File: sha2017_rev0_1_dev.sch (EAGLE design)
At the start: 87 parts, among them IC1 AP7215, IC2 LM1117, IC3 CP210X_USB_UART, IC5 ESP32WROOM32, Q1 MMBT2222A, Q2 MMBT2222A, Q3 SI1304 BDL, SW100 MCMT5-F-V, X701 2908-05WB-MG

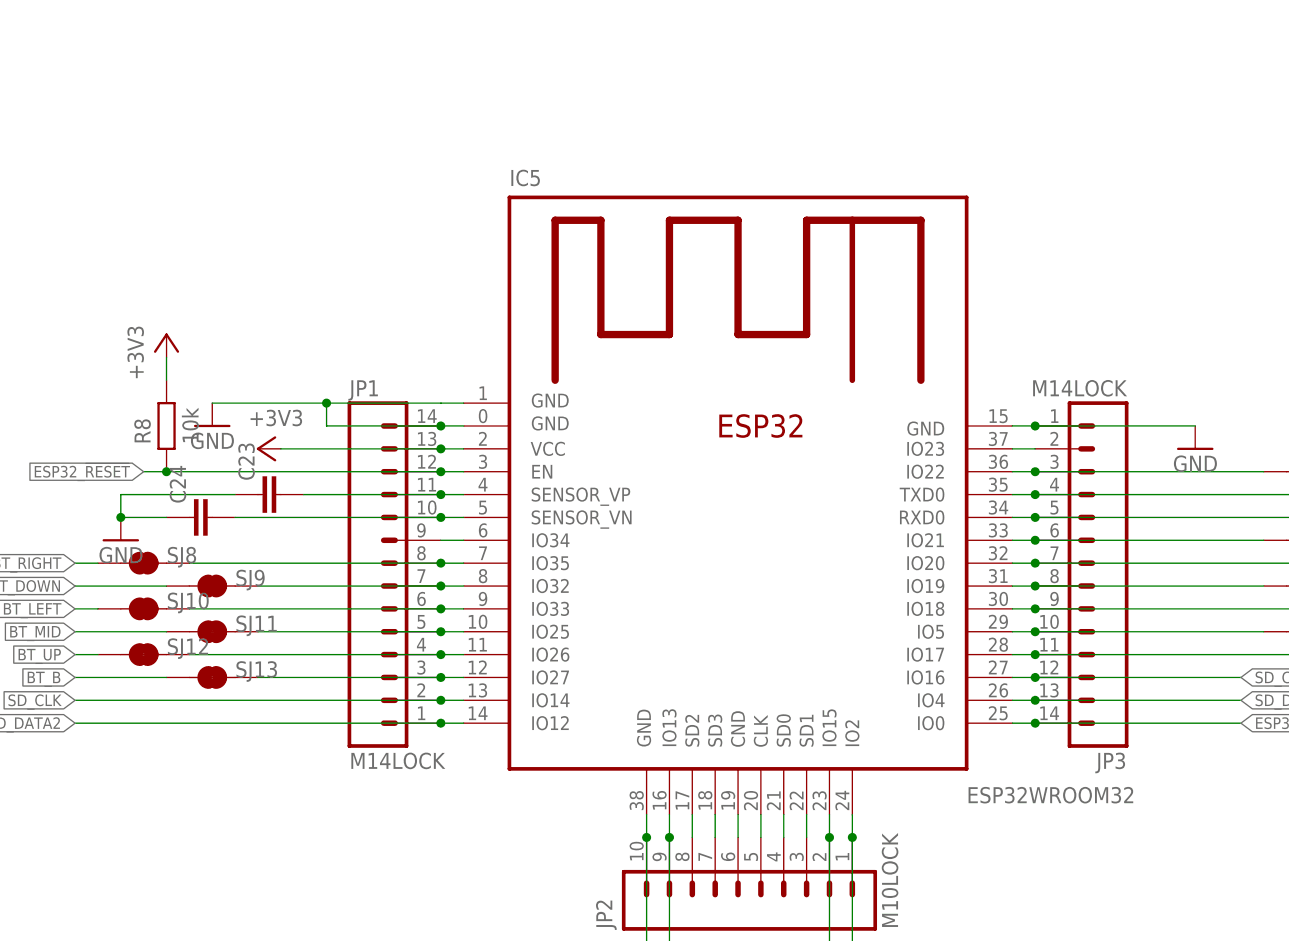
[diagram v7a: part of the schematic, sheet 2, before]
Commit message: fixed silkscreen
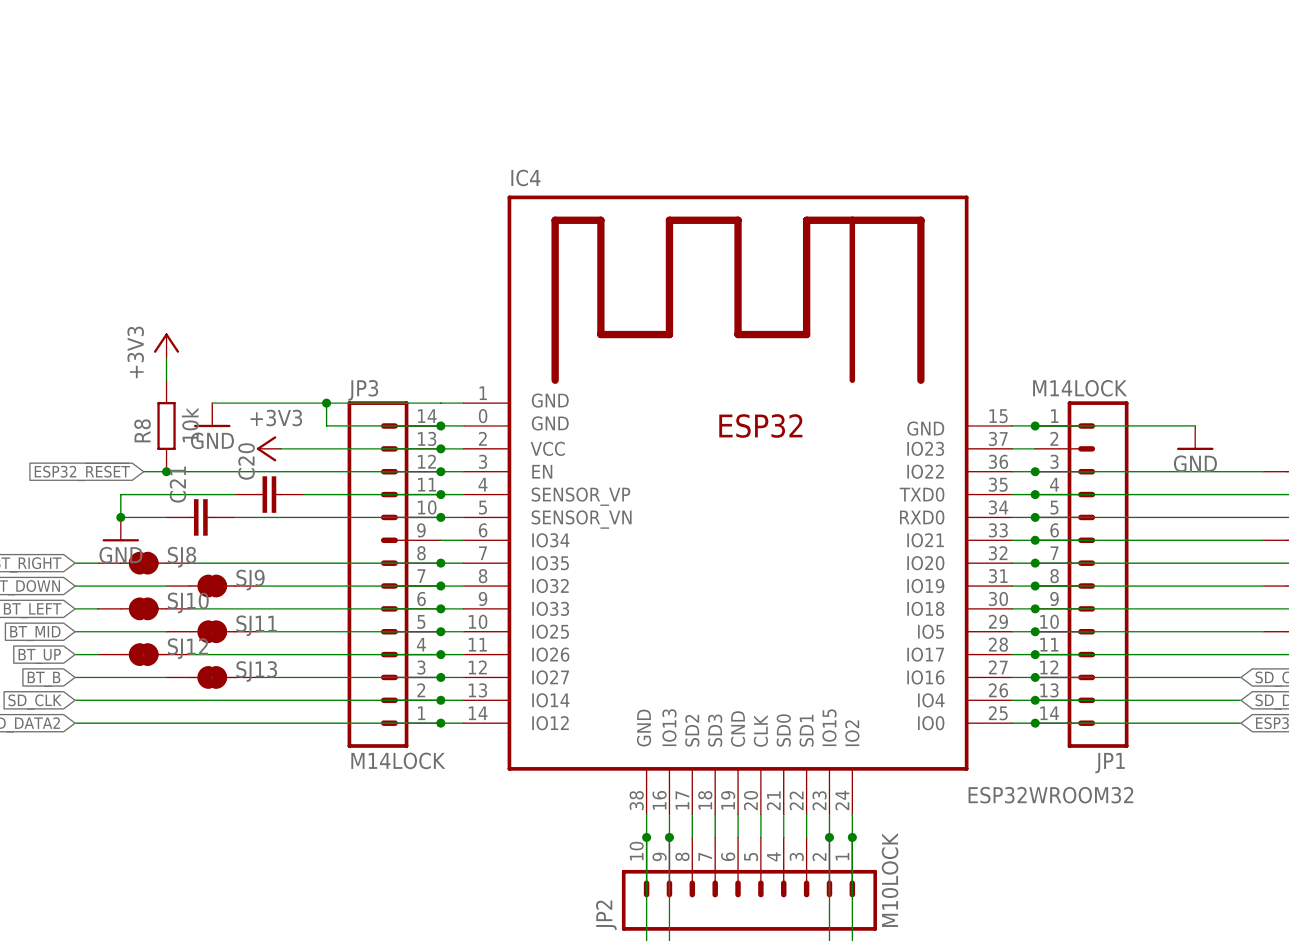
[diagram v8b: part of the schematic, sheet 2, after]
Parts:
- C20: value 100n -> (none); OC_FARNELL (none) -> unknown; PARTNO GRM188R71H104KA93D -> (none)
- C21: value 4u7/16V -> (none); device rcl:C-EUC0805 -> rcl:C-EUC0603; OC_FARNELL (none) -> unknown; PARTNO GRM21BR61C475KA88K -> (none)
- C23: value (none) -> 4u7/16V; device rcl:C-EUC0603 -> rcl:C-EUC0805; OC_FARNELL unknown -> (none); PARTNO (none) -> GRM21BR61C475KA88K
- C24: value (none) -> 100n; OC_FARNELL unknown -> (none); PARTNO (none) -> GRM188R71H104KA93D
- renumbered D100 to D8, IC5 to IC4
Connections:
- net +3V3: now also C23.1, C24.1, JP3.13; no longer C20.1, C21.1, JP1.13
- net ESP32_!RESET: now also JP3.12; no longer JP1.12
- net ESP32_FLASH/TOUCHE_MENU: now also JP1.14; no longer JP3.14
- net ESP32_RX: now also JP1.5; no longer JP3.5
- net ESP32_TX: now also JP1.4; no longer JP3.4
- net GND: now also C20.1, C21.1, C23.2, C24.2, JP1.1, JP3.14; no longer C20.2, C21.2, C23.1, C24.1, JP1.14, JP3.1
- net N$1: now also JP3.9; no longer JP1.9
- net N$15: now also JP1.2; no longer JP3.2
- net N$16: now also JP1.3; no longer JP3.3
- net N$17: now also JP1.6; no longer JP3.6
- net N$18: now also JP1.7; no longer JP3.7
- net N$20: now also JP1.9; no longer JP3.9
- net N$21: now also JP1.10; no longer JP3.10
- net N$24: now also JP1.11; no longer JP3.11
- net N$42: now also C20.2, JP3.11; no longer C23.2, JP1.11
- net N$43: now also C21.2, JP3.10; no longer C24.2, JP1.10
- net N$44: now also JP3.8; no longer JP1.8
- net N$45: now also JP3.7; no longer JP1.7
- net N$46: now also JP3.6; no longer JP1.6
- net N$47: now also JP3.5; no longer JP1.5
- net N$48: now also JP3.4; no longer JP1.4
- net N$49: now also JP3.3; no longer JP1.3
- net N$63: now also JP1.8; no longer JP3.8
- net SD_CD: now also JP1.12; no longer JP3.12
- net SD_CLK: now also JP3.2; no longer JP1.2
- net SD_DATA1: now also JP1.13; no longer JP3.13
- net SD_DATA2: now also JP3.1; no longer JP1.1
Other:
- moved on the sheet: JP1, JP3
